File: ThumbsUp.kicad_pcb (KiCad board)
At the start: 2 copper layers, 222.3 x 198.8 mm, 44 parts, among them J10 Raiser_Male, J13 Raiser_Female, J14 Raiser_Male, J19 Raiser_Female, J1L1 PJ-3200B, J1R1 PJ-3200B, J33 Raiser_Male, J34 Raiser_Female, J35 Raiser_Male, J38 Raiser_Female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

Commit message: K12: Modifying the layout, WIP.
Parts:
- removed G*** (x2): LOGO, Silkscreens:Crowfeet
- removed H12, H3: MountingHole_Pad, MountingHole:MountingHole_3.5mm_Pad
- added ?: , , F.Cu at (43.0, 66.4)
- added JP1: Handiness, Jumper:SolderJumper-2_P1.3mm_Open_RoundedPad1.0x1.5mm, F.Cu at (78.7, 25.4)
- moved J48 61.7 mm to (91.3, 220.9), turned to 90 degrees
- moved J47 59.8 mm to (91.3, 101.0), turned to -90 degrees
- moved J40 28.7 mm to (57.9, 83.2), turned to -65 degrees
- moved STUDIO_UNLOCK2 24.9 mm to (45.3, 49.4), turned to 90 degrees
- moved STUDIO_UNLOCK1 24.8 mm to (45.4, 49.4), turned to -90 degrees
- moved MX23 24.5 mm to (54.2, 66.4), turned to 90 degrees
- moved J38 19.8 mm to (39.6, 32.4)
- moved MX26 19.3 mm to (63.4, 90.1), turned to 25 degrees
- moved MX30 19.3 mm to (49.3, 96.7), turned to 25 degrees
- moved J10 19.2 mm to (148.3, 149.0)
- moved J35 19.2 mm to (164.5, 179.4)
- moved J14 19.2 mm to (138.3, 221.0)
- moved H1 18.3 mm to (134.9, 151.7)
- moved H2 17.7 mm to (103.1, 215.3)
- moved J33 17.7 mm to (99.1, 143.0)
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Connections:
- J47 pad 1: L-BASE -> (no net)
- J47 pad 2: L-BASE -> (no net)
- J47 pad 3: L-BASE -> (no net)
- J47 pad 4: L-BASE -> (no net)
- J48 pad 1: GNDA -> (no net)
- J48 pad 2: GNDA -> (no net)
- J48 pad 3: GNDA -> (no net)
- J48 pad 4: GNDA -> (no net)
- U1 pad 7: unconnected-(U1-D4-Pad7) -> Net-(JP1-B)
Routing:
- net SwZ: track 120.7 -> 0.00 mm
- net SwS: track 111.9 -> 0.00 mm
- net SwD: track 105.1 -> 0.00 mm
- net SwG: track 102.3 -> 0.00 mm
- net SwT: track 89.2 -> 0.00 mm
- net SwB: track 81.9 -> 0.00 mm
- net SwL: track 77.2 -> 0.00 mm
- net SwR: track 69.4 -> 0.00 mm
- net SwU: track 64.7 -> 0.00 mm
- net SwE: track 64.0 -> 0.00 mm
- net SwP: track 55.5 -> 0.00 mm
- net SwF: track 34.8 -> 0.00 mm
- net L-RING1: track 29.0 -> 0.00 mm
- net RESET: track 26.6 -> 0.00 mm
- net L-TIP: track 21.0 -> 0.00 mm
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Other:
- board size 222.3 x 198.8 mm -> 209.3 x 201 mm
- board text added: "Raiser_Female"

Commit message: K12: Modifying the layout, WIP.
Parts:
- removed ?: , 
- added H12: MountingHole_Pad, MountingHole:MountingHole_3.5mm_Pad, F.Cu at (152.0, 98.6)
- added H3: MountingHole_Pad, MountingHole:MountingHole_3.5mm_Pad, F.Cu at (42.9, 66.4)
- added H6: MountingHole_Pad, MountingHole:MountingHole_3.5mm_Pad, F.Cu at (152.0, 218.6)
- JP1: moved to B.Cu
- moved JP1 26.7 mm to (59.2, 43.6), turned to 180 degrees
- moved H4 6.45 mm to (93.6, 65.1)
- moved J14 5.60 mm to (132.7, 221.0)
- moved J13 5.60 mm to (132.7, 101.0)
- moved STUDIO_UNLOCK1 3.37 mm to (42.0, 49.4)
- moved STUDIO_UNLOCK2 3.32 mm to (42.0, 49.4)
- moved J1L1 0.50 mm to (47.0, 23.2)
- moved J1R1 0.50 mm to (44.9, 23.2)
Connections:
- J47 pad 1: (no net) -> L-BASE
- J47 pad 2: (no net) -> L-BASE
- J47 pad 3: (no net) -> L-BASE
- J47 pad 4: (no net) -> L-BASE
- J48 pad 1: (no net) -> GNDA
- J48 pad 2: (no net) -> GNDA
- J48 pad 3: (no net) -> GNDA
- J48 pad 4: (no net) -> GNDA
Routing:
- net SwZ: track 0.00 -> 115.1 mm
- net SwG: track 0.00 -> 112.0 mm
- net SwS: track 0.00 -> 111.1 mm
- net SwD: track 0.00 -> 95.2 mm
- net SwB: track 0.00 -> 90.5 mm, vias 0 -> 1
- net SwE: track 0.00 -> 77.3 mm, vias 0 -> 1
- net SwT: track 0.00 -> 77.3 mm
- net SwR: track 0.00 -> 69.9 mm, vias 0 -> 1
- net SwU: track 0.00 -> 62.9 mm, vias 0 -> 1
- net SwL: track 0.00 -> 62.5 mm
- net RESET: track 0.00 -> 52.9 mm, vias 0 -> 1
- net SwP: track 0.00 -> 40.4 mm
- net SwAst: track 0.00 -> 34.9 mm, vias 0 -> 1
- net L-RING1: track 0.00 -> 26.8 mm
- net SwF: track 0.00 -> 22.9 mm
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- added copper zone on B.Cu, net (none)
- added copper zone on F.Cu, net (none)
- removed copper zone on B.Cu, net GNDB
- removed copper zone on F.Cu, net GNDB
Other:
- board text added: "CLOSE FOR RIGHT HAND"

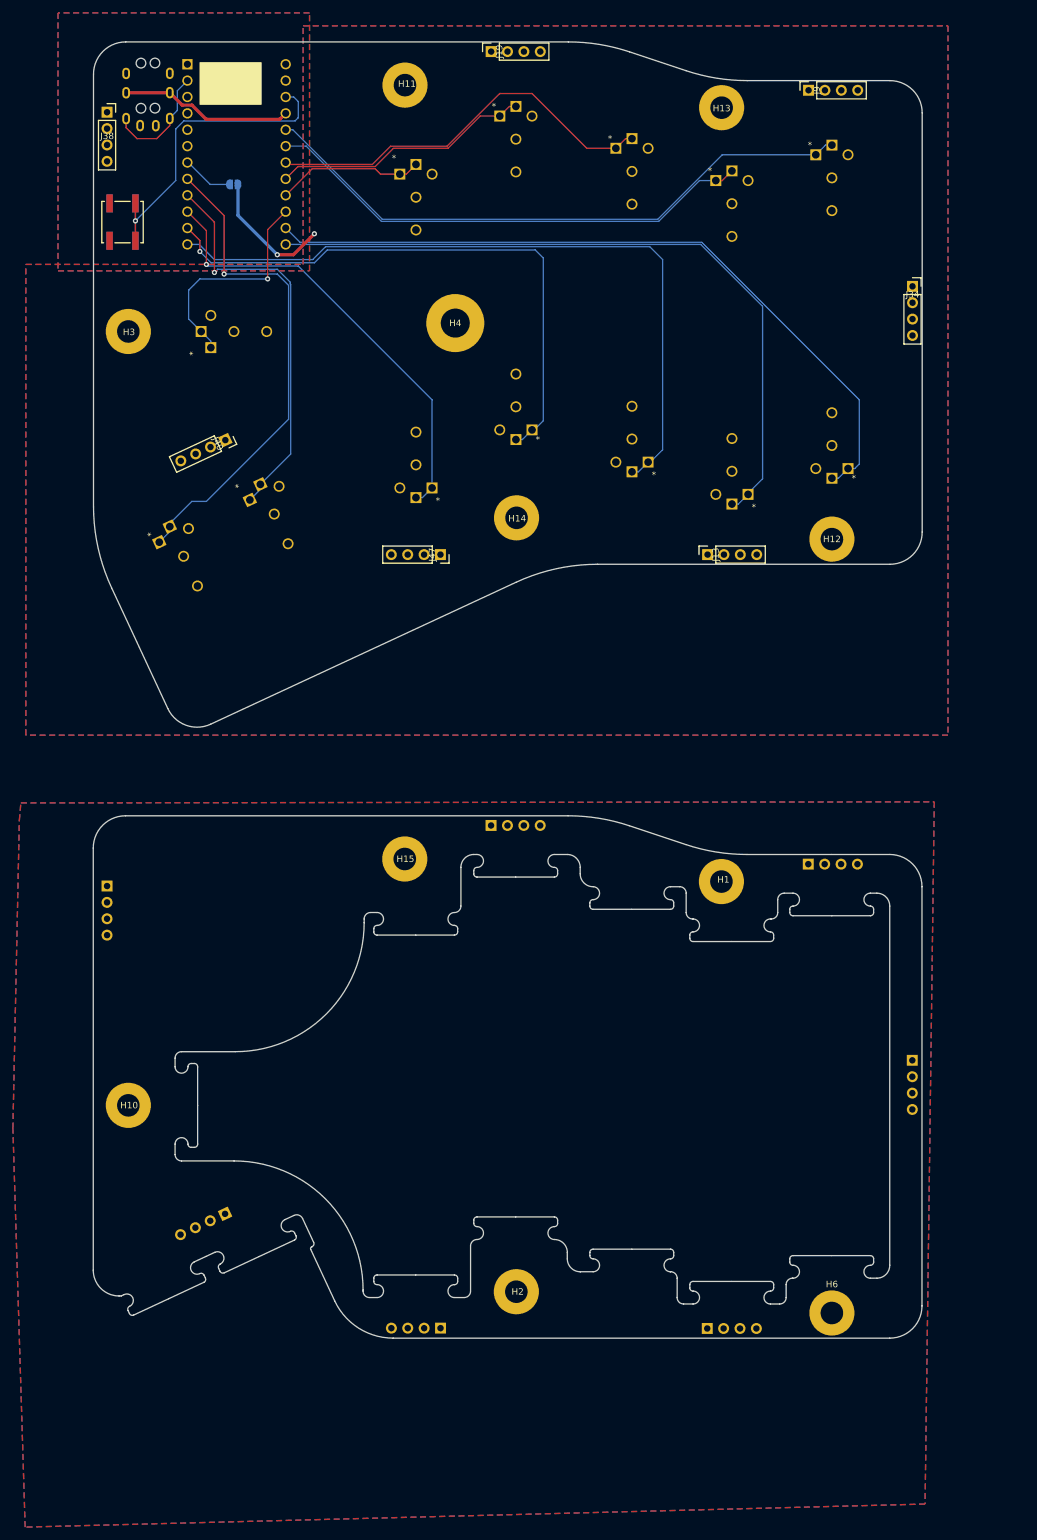
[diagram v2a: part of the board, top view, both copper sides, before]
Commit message: K12: Changed layout as per rev.1 usage experience.
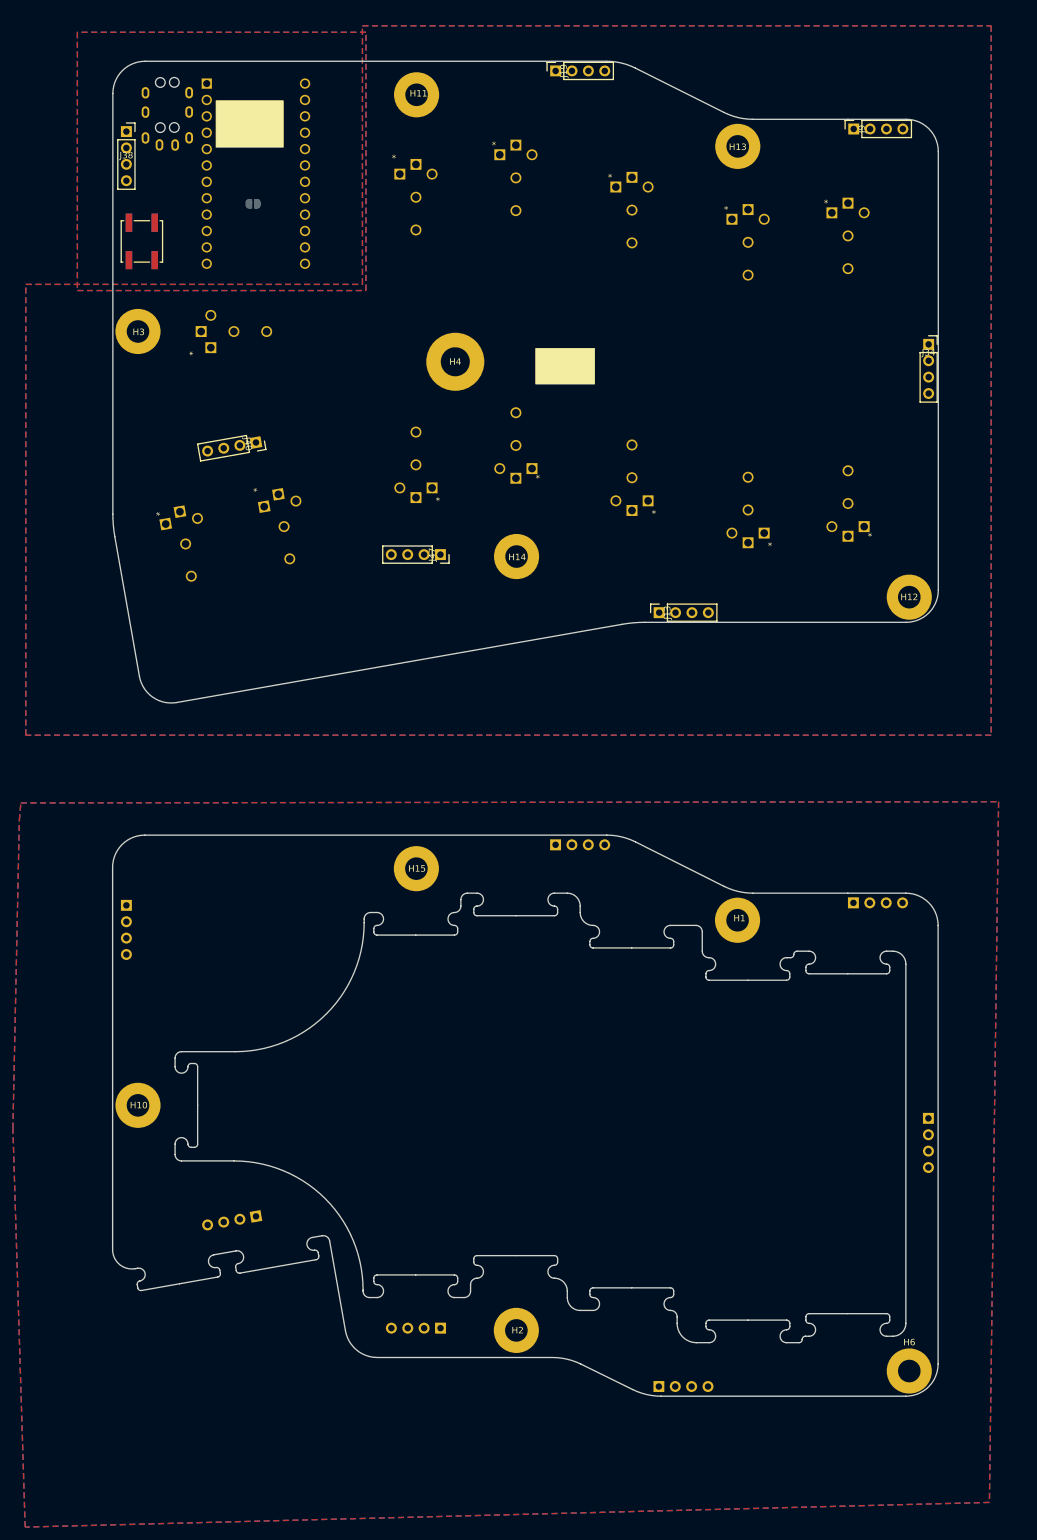
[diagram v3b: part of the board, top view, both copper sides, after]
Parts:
- moved H12 15.0 mm to (164.0, 107.6)
- moved H6 15.0 mm to (164.0, 227.6)
- moved J13 11.7 mm to (125.2, 110.0)
- moved J14 11.7 mm to (125.2, 230.0)
- moved J19 10.4 mm to (109.2, 26.0)
- moved J33 10.4 mm to (109.1, 146.0)
- moved J34 9.34 mm to (167.0, 68.4)
- moved J35 9.34 mm to (167.0, 188.4)
- moved MX42 9.34 mm to (154.5, 46.5)
- moved MX43 9.34 mm to (154.5, 98.2)
- moved J10 9.22 mm to (155.3, 155.0)
- moved J9 9.22 mm to (155.4, 35.0)
- moved H13 6.50 mm to (137.4, 37.7)
- moved H1 6.50 mm to (137.4, 157.7)
- moved MX39 6.50 mm to (139.0, 47.5)
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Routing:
- net SwZ: track 115.1 -> 0.00 mm
- net SwG: track 112.0 -> 0.00 mm
- net SwS: track 111.1 -> 0.00 mm
- net SwD: track 95.2 -> 0.00 mm
- net SwB: track 90.5 -> 0.00 mm, vias 1 -> 0
- net SwE: track 77.3 -> 0.00 mm, vias 1 -> 0
- net SwT: track 77.3 -> 0.00 mm
- net SwR: track 69.9 -> 0.00 mm, vias 1 -> 0
- net SwU: track 62.9 -> 0.00 mm, vias 1 -> 0
- net SwL: track 62.5 -> 0.00 mm
- net RESET: track 52.9 -> 0.00 mm, vias 1 -> 0
- net SwP: track 40.4 -> 0.00 mm
- net SwAst: track 34.9 -> 0.00 mm, vias 1 -> 0
- net L-RING1: track 26.8 -> 0.00 mm
- net SwF: track 22.9 -> 0.00 mm
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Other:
- board size 209.3 x 201 mm -> 206.3 x 207 mm
- board text added: "u/ak66666 ThumbsUp! v.12 rev.2"

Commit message: K12: Added left-side handiness pull-up R, laid out all tracks. TODO: generate Gerbers.
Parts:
- added R17: 5.1K, Resistor_SMD:R_0805_2012Metric, B.Cu at (64.6, 32.2)
- JP1: value Handiness -> Right Hand
- moved JP1 1.31 mm to (62.9, 47.8)
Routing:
- net SwZ: track 0.00 -> 118.8 mm
- net SwS: track 0.00 -> 110.3 mm
- net SwD: track 0.00 -> 101.4 mm, vias 0 -> 1
- net SwG: track 0.00 -> 98.5 mm
- net SwB: track 0.00 -> 93.5 mm
- net SwT: track 0.00 -> 82.0 mm, vias 0 -> 1
- net SwR: track 0.00 -> 67.9 mm
- net SwL: track 0.00 -> 62.7 mm, vias 0 -> 1
- net RESET: track 0.00 -> 61.9 mm, vias 0 -> 1
- net SwE: track 0.00 -> 53.3 mm
- net SwU: track 0.00 -> 53.0 mm
- net SwP: track 0.00 -> 48.3 mm, vias 0 -> 1
- net SwAst: track 0.00 -> 34.2 mm
- net L-RING1: track 0.00 -> 28.2 mm
- net Net-(JP1-B): track 0.00 -> 27.7 mm, vias 0 -> 1
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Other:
- board text added: "LEFT HAND 5.1K"

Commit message: K12: Doing modifications outlined for rev.3
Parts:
- R17: moved to F.Cu
- moved R17 47.8 mm to (17.3, 39.2)
- moved J41 26.1 mm to (57.9, 229.2), turned to 115 degrees
- moved J48 26.0 mm to (91.3, 246.9)
- moved H10 21.4 mm to (36.9, 206.4)
- moved H6 20.8 mm to (152.0, 244.6)
- moved H2 20.0 mm to (103.1, 241.3)
- moved J14 18.6 mm to (132.7, 247.0)
- moved MX30 18.4 mm to (49.3, 112.7), turned to 25 degrees
- moved J40 16.3 mm to (57.9, 99.2), turned to -65 degrees
- moved J47 16.0 mm to (91.3, 117.0)
- moved MX28 16.0 mm to (87.5, 108.2)
- moved J33 14.9 mm to (99.1, 157.0)
- moved MX26 14.7 mm to (63.4, 106.1), turned to 25 degrees
- moved J39 14.2 mm to (33.6, 166.4)
- moved H12 13.9 mm to (152.0, 114.6)
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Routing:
- net SwE: track 53.3 -> 103.6 mm, vias 0 -> 1
- net GND-P: track 0.00 -> 44.5 mm
- net Net-(JP1-B): track 27.7 -> 7.95 mm, vias 1 -> 0
- net SwU: track 53.0 -> 36.6 mm, vias 0 -> 1
- net SwG: track 98.5 -> 112.0 mm
- net L-BASE: track 9.98 -> 20.5 mm, vias 1 -> 2
- net RESET: track 61.9 -> 52.9 mm
- net SwP: track 48.3 -> 40.4 mm, vias 1 -> 0
- net SwD: track 101.4 -> 95.2 mm, vias 1 -> 0
- net SwT: track 82.0 -> 77.3 mm, vias 1 -> 0
- net L-TIP: track 14.1 -> 18.2 mm
- net SwZ: track 118.8 -> 115.1 mm
- net SwB: track 93.5 -> 90.5 mm, vias 0 -> 1
- net SwF: track 20.4 -> 22.9 mm
- net SwR: track 67.9 -> 69.9 mm, vias 0 -> 1
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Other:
- board size 206.3 x 207 mm -> 215.3 x 223 mm
- board text removed: "LEFT HAND 5.1K"
- board text removed: "u/ak66666 ThumbsUp! v.12 rev.2"

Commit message: K12: Placed the touchpad, todo: tracks
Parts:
- added J1: 52559-1233, KiCad:525591233, B.Cu at (39.5, 48.6)
- added J2: 52559-1233, KiCad:525591233, F.Cu at (39.5, 48.6)
- added R1: 4.7k, Resistor_SMD:R_0805_2012Metric, B.Cu at (54.0, 53.0)
- added R2: 4.7k, Resistor_SMD:R_0805_2012Metric, B.Cu at (54.0, 56.0)
- added R4: 4.7k, Resistor_SMD:R_0805_2012Metric, F.Cu at (54.3, 55.9)
- added R5: 4.7k, Resistor_SMD:R_0805_2012Metric, F.Cu at (54.3, 53.0)
- R17: moved to B.Cu
- moved STUDIO_UNLOCK2 42.9 mm to (72.0, 30.0), turned to 0 degrees
- moved STUDIO_UNLOCK1 42.9 mm to (72.0, 30.0), turned to 180 degrees
- moved R17 38.1 mm to (53.9, 49.8), turned to 180 degrees
- moved J13 7.00 mm to (125.7, 117.0)
- moved J14 7.00 mm to (125.7, 247.0)
- moved J38 5.00 mm to (33.6, 31.4)
- moved J39 5.00 mm to (33.6, 161.4)
- moved JP1 2.05 mm to (54.0, 45.7)
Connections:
- net L-BASE renamed GND
- U1 pad 5: unconnected-(U1-SDA-Pad5) -> SDA
- U1 pad 6: unconnected-(U1-SCL-Pad6) -> SCL
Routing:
- net SwZ: track 115.1 -> 0.00 mm
- net SwG: track 112.0 -> 0.00 mm
- net SwS: track 111.1 -> 0.00 mm
- net SwE: track 103.6 -> 0.00 mm, vias 1 -> 0
- net SwD: track 95.2 -> 0.00 mm
- net SwB: track 90.5 -> 0.00 mm, vias 1 -> 0
- net SwT: track 77.3 -> 0.00 mm
- net SwR: track 69.9 -> 0.00 mm, vias 1 -> 0
- net SwL: track 62.5 -> 0.00 mm
- net RESET: track 52.9 -> 0.00 mm, vias 1 -> 0
- net GND-P: track 44.5 -> 0.00 mm
- net (no net): track 0.00 -> 44.5 mm
- net SwP: track 40.4 -> 0.00 mm
- net SwU: track 36.6 -> 0.00 mm, vias 1 -> 0
- net SwAst: track 34.9 -> 0.00 mm, vias 1 -> 0
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- removed copper zone on B.Cu, net GND
- removed copper zone on F.Cu, net GND
- removed copper zone on B.Cu, net GNDA
- removed copper zone on F.Cu, net GNDA
